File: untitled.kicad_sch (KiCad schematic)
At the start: 27 parts, among them J10 IN 1x6h, J11 SYNC, J12 PWM, J13 CV, J14 1VOct, J15 FM, J17 OCT_SW 1x7h, J19 CV 1x6h, J2 SQR, J3 OUT 1x4h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

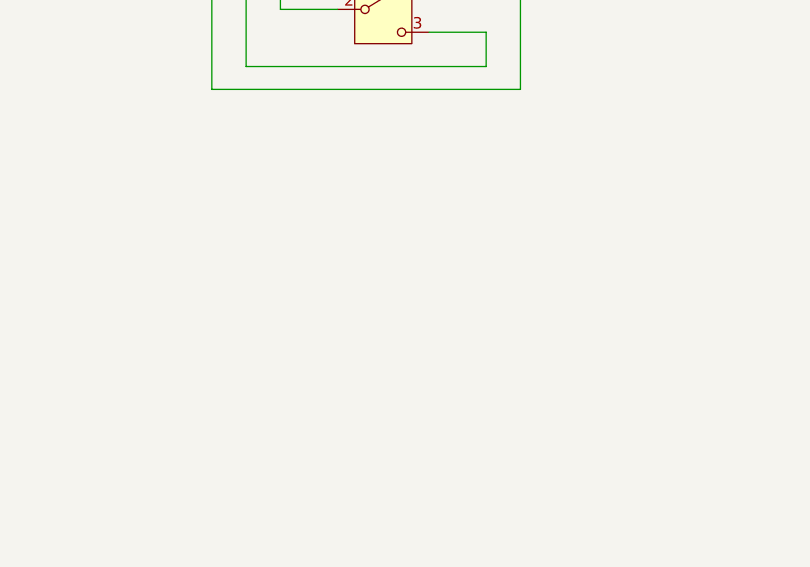
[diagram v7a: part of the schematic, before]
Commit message: Moved LED to control board.
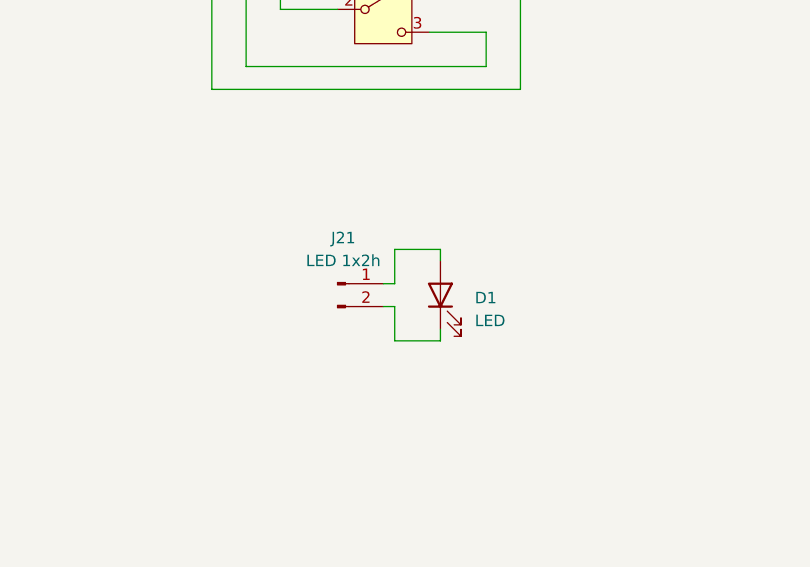
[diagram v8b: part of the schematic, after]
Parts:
- added D1: LED, symbol Device:LED
- added J21: LED 1x2h, symbol Connector:Conn_01x02_Pin
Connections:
- new net: D1.2 (A), J21.1 (Pin_1)
- new net: D1.1 (K), J21.2 (Pin_2)
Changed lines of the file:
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@@
 	(wire
 		(pts
+			(xy 199.39 134.62) (xy 199.39 138.43)
+		)
+		(stroke
+			(width 0)
+			(type default)
+		)
+	)
+	(wire
+		(pts
 			(xy 264.16 110.49) (xy 264.16 105.41)
 		)
@@
 	(wire
 		(pts
+			(xy 198.12 138.43) (xy 199.39 138.43)
+		)
+		(stroke
+			(width 0)
+			(type default)
+		)
+	)
+	(wire
+		(pts
 			(xy 107.95 63.5) (xy 120.65 63.5)
 		)
@@
 	(wire
 		(pts
+			(xy 204.47 135.89) (xy 204.47 134.62)
+		)
+		(stroke
+			(width 0)
+			(type default)
+		)
+	)
+	(wire
+		(pts
+			(xy 204.47 134.62) (xy 199.39 134.62)
+		)
+		(stroke
+			(width 0)
+			(type default)
+		)
+	)
+	(wire
+		(pts
 			(xy 264.16 72.39) (xy 261.62 72.39)
 		)
@@
 	(wire
 		(pts
+			(xy 198.12 140.97) (xy 199.39 140.97)
+		)
+		(stroke
+			(width 0)
+			(type default)
+		)
+	)
+	(wire
+		(pts
 			(xy 30.48 110.49) (xy 33.02 110.49)
 		)
@@
 	(wire
 		(pts
+			(xy 199.39 140.97) (xy 199.39 144.78)
+		)
+		(stroke
+			(width 0)
+			(type default)
+		)
+	)
+	(wire
+		(pts
 			(xy 62.23 95.25) (xy 45.72 95.25)
 		)
@@
 		)
 	)
+	(wire
+		(pts
+			(xy 204.47 143.51) (xy 204.47 144.78)
+		)
+		(stroke
+			(width 0)
+			(type default)
+		)
+	)
+	(wire
+		(pts
+			(xy 199.39 144.78) (xy 204.47 144.78)
+		)
+		(stroke
+			(width 0)
+			(type default)
+		)
+	)
 	(symbol
 		(lib_id "Connector_Audio:AudioJack2_SwitchT")
@@
 	)
 	(symbol
+		(lib_id "Connector:Conn_01x02_Pin")
+		(at 193.04 138.43 0)
+		(unit 1)
+		(exclude_from_sim no)
+		(in_bom yes)
+		(on_board yes)
+		(dnp no)
+		(fields_autoplaced yes)
+		(property "Reference" "J21"
+			(at 193.675 133.35 0)
+			(effects
+				(font
+					(size 1.27 1.27)
+				)
+			)
+		)
+		(property "Value" "LED 1x2h"
+			(at 193.675 135.89 0)
+			(effects
+				(font
+					(size 1.27 1.27)
+				)
+			)
+		)
+		(property "Footprint" ""
+			(at 193.04 138.43 0)
+			(effects
+				(font
+					(size 1.27 1.27)
+				)
+				(hide yes)
+			)
+		)
+		(property "Datasheet" "~"
+			(at 193.04 138.43 0)
+			(effects
+				(font
+					(size 1.27 1.27)
+				)
+				(hide yes)
+			)
+		)
+		(property "Description" "Generic connector, single row, 01x02, script generated"
+			(at 193.04 138.43 0)
+			(effects
+				(font
+					(size 1.27 1.27)
+				)
+				(hide yes)
+			)
+		)
+		(pin "1"
+		)
+		(pin "2"
+		)
+		(instances
+			(project ""
+				(path "/eb1652b6-57da-4a0e-88a4-449907a19840/2395376b-3fab-44b6-8171-4759de5684a3"
+					(reference "J21")
+					(unit 1)
+				)
+			)
+		)
+	)
+	(symbol
 		(lib_id "power:GND")
 		(at 134.62 100.33 0)
@@
 					(unit 1)
 				)
+			)
+		)
+	)
+	(symbol
+		(lib_id "Device:LED")
+		(at 204.47 139.7 90)
+		(unit 1)
+		(exclude_from_sim no)
+		(in_bom yes)
+		(on_board yes)
+		(dnp no)
+		(fields_autoplaced yes)
+		(property "Reference" "D1"
+			(at 208.28 140.0174 90)
+			(effects
+				(font
+					(size 1.27 1.27)
+				)
+				(justify right)
+			)
+		)
+		(property "Value" "LED"
+			(at 208.28 142.5574 90)
+			(effects
+				(font
+					(size 1.27 1.27)
+				)
+				(justify right)
+			)
+		)
+		(property "Footprint" ""
+			(at 204.47 139.7 0)
+			(effects
+				(font
+					(size 1.27 1.27)
+				)
+				(hide yes)
+			)
+		)
+		(property "Datasheet" "~"
+			(at 204.47 139.7 0)
+			(effects
+				(font
+					(size 1.27 1.27)
+				)
+				(hide yes)
+			)
+		)
+		(property "Description" "Light emitting diode"
+			(at 204.47 139.7 0)
+			(effects
+				(font
+					(size 1.27 1.27)
+				)
+				(hide yes)
+			)
+		)
+		(property "Sim.Pins" "1=K 2=A"
+			(at 204.47 139.7 0)
+			(effects
+				(font
+					(size 1.27 1.27)
+				)
+				(hide yes)
+			)
+		)
+		(pin "2"
+		)
+		(pin "1"
+		)
+		(instances
+			(project "VCO 2"
+				(path "/eb1652b6-57da-4a0e-88a4-449907a19840/2395376b-3fab-44b6-8171-4759de5684a3"
+					(reference "D1")
+					(unit 1)
+				)
